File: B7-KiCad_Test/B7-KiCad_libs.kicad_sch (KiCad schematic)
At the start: 1 part, among them U1 STM32F446VETx

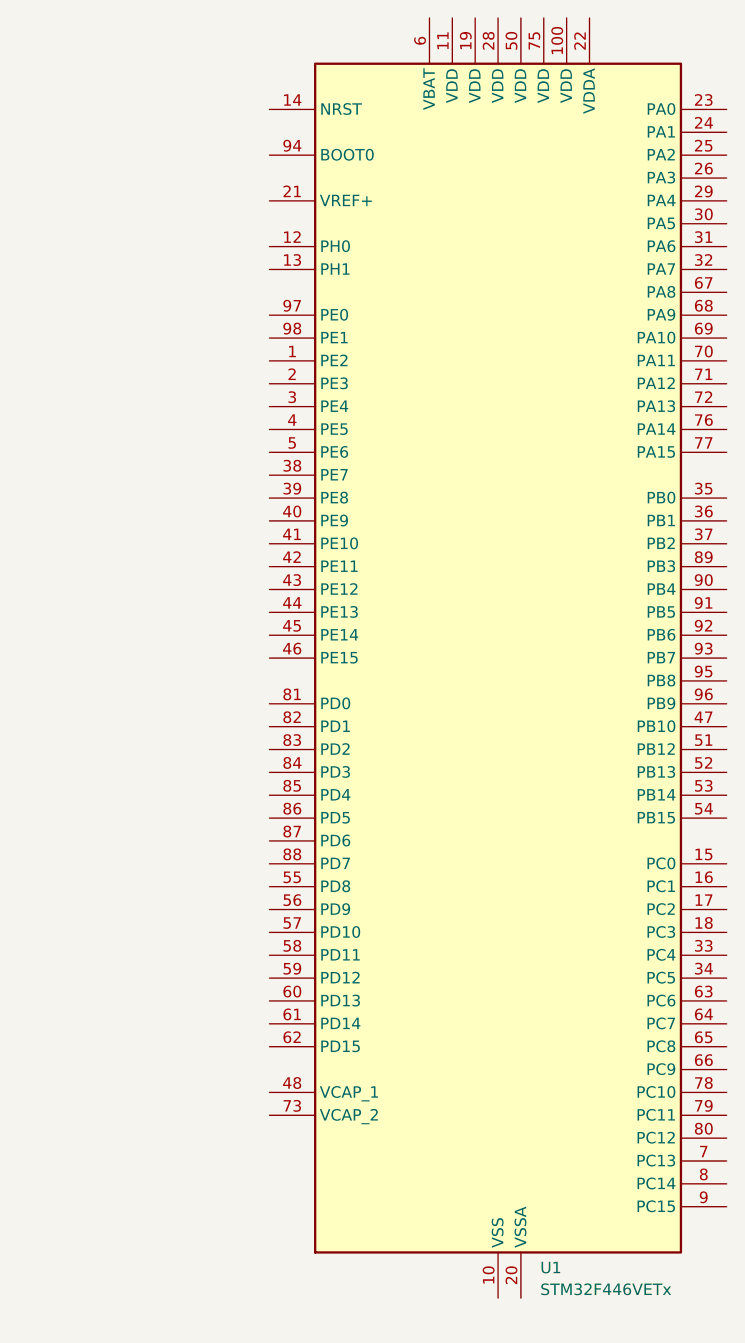
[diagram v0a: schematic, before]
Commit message: partd aus Projektverzeichnis raus genommen
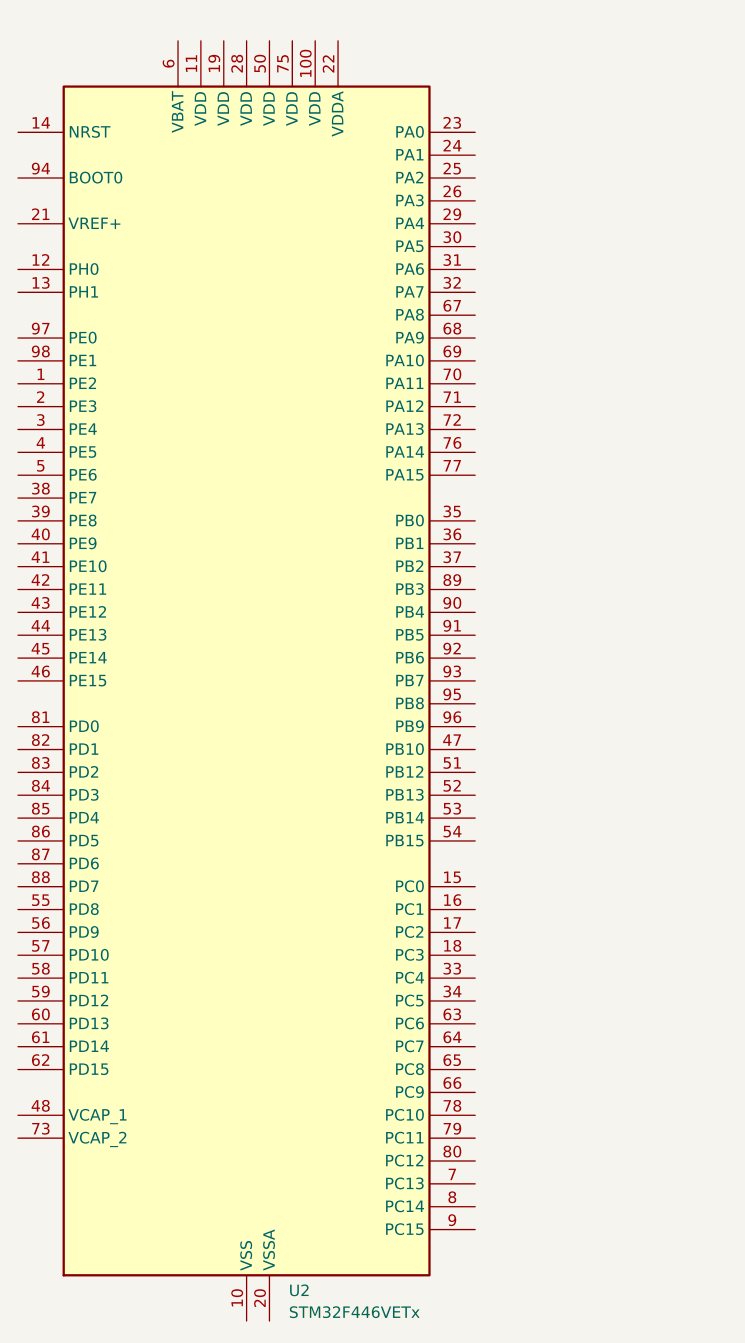
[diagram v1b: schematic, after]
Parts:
- removed U1: STM32F446VETx, Package_QFP:LQFP-100_14x14mm_P0.5mm, symbol partd:STM32F446VET6TR
- added U2: STM32F446VETx, Package_QFP:LQFP-100_14x14mm_P0.5mm, symbol B7-resistor_SMD:STM32F446VETx
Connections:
- new net: U2.10 (VSS), U2.27 (VSS), U2.49 (VSS), U2.74 (VSS), U2.99 (VSS)
